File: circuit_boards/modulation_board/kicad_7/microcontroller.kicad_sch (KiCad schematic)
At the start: 27 parts, among them J301 SWD_header, U1 STM32L412K8Ux, U2 VO0600T, U3 SN74LV1T34DBV, Y301 32_768KHZ

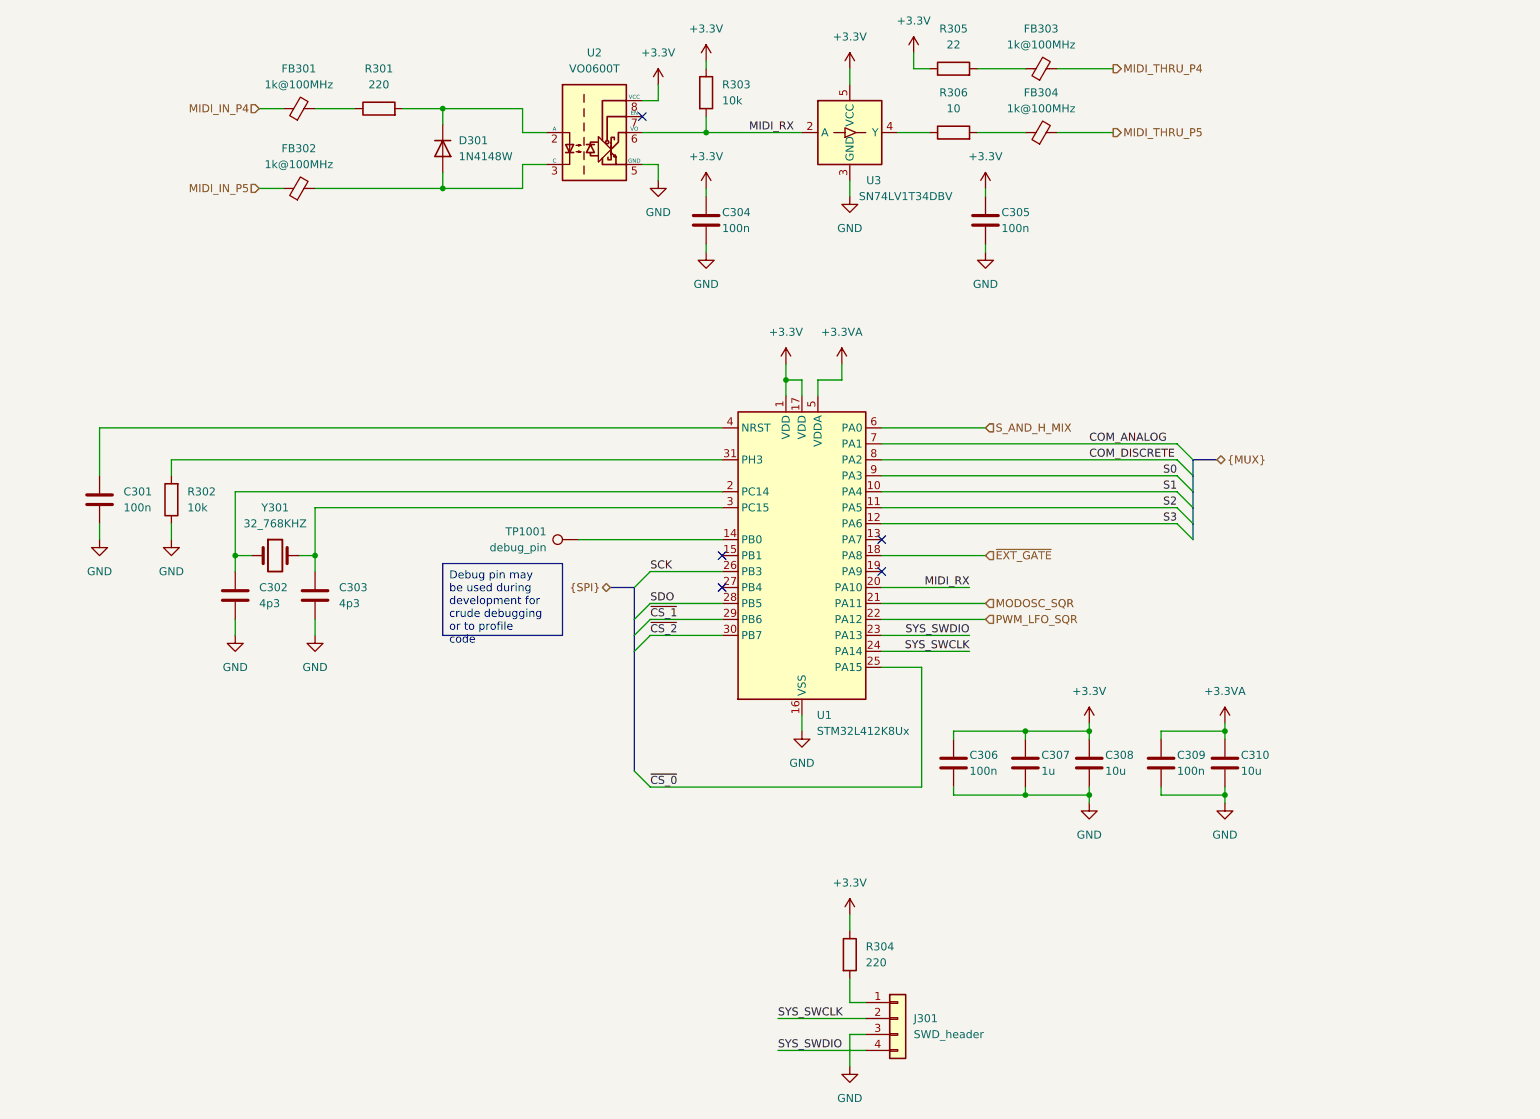
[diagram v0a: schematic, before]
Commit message: Tweaks to mod board, debounce MODOSC toggle switch
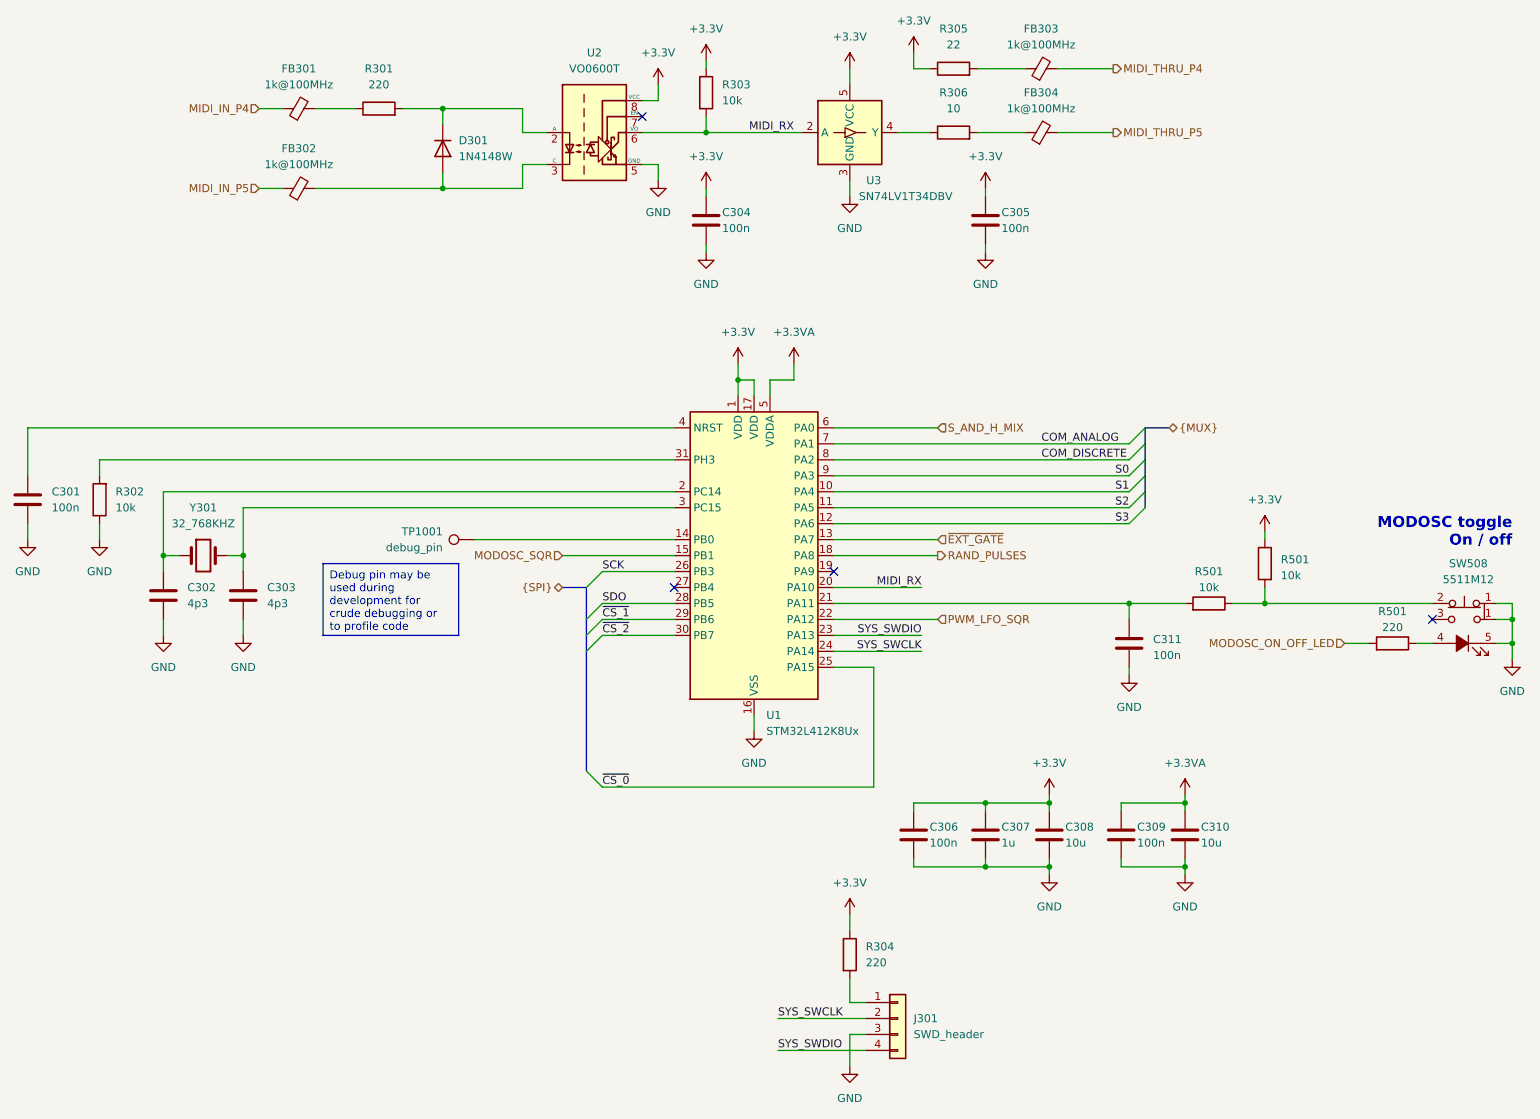
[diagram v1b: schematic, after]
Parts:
- removed U1: STM32L412K8Ux, Package_DFN_QFN:QFN-32-1EP_5x5mm_P0.5mm_EP3.45x3.45mm, symbol MCU_ST_STM32L4:STM32L412K8Ux
- added C311: 100n, Capacitor_SMD:C_0603_1608Metric, symbol Device:C
- added R501 (x2): 10k, Resistor_SMD:R_0603_1608Metric, symbol Device:R
- added R501: 220, Resistor_SMD:R_0603_1608Metric, symbol Device:R
- added SW508: 5511M12, custom_footprints:E_Switch_5511M12, symbol custom_symbols:E_Switch_5511M12
- added U1: STM32L412K8Ux, Package_DFN_QFN:QFN-32-1EP_5x5mm_P0.5mm_EP3.45x3.45mm, symbol custom_symbols:STM32L412K8Ux
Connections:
- net +3.3V: now also R501.1, U1.1 (VDD), U1.17 (VDD)
- net +3.3VA: now also U1.5 (VDDA)
- net COM_ANALOG: now also U1.7 (PA1)
- net COM_DISCRETE: now also U1.8 (PA2)
- net GND: now also C311.1, SW508.1, SW508.5, U1.16 (VSS), U1.32 (VSS), U1.33 (VSS)
- net MIDI_RX: now also U1.20 (PA10)
- net MODOSC_SQR: now also U1.15 (PB1)
- net PWM_LFO_SQR: now also U1.22 (PA12)
- net S0: now also U1.9 (PA3)
- net S1: now also U1.10 (PA4)
- net S2: now also U1.11 (PA5)
- net S3: now also U1.12 (PA6)
- net SCK: now also U1.26 (PB3)
- net SDO: now also U1.28 (PB5)
- net SYS_SWCLK: now also U1.24 (PA14)
- net SYS_SWDIO: now also U1.23 (PA13)
- net S_AND_H_MIX: now also U1.6 (PA0)
- net ~{CS_0}: now also U1.25 (PA15)
- net ~{CS_1}: now also U1.29 (PB6)
- net ~{CS_2}: now also U1.30 (PB7)
- net ~{EXT_GATE}: now also U1.13 (PA7)
- net at C301.2: now also U1.4 (NRST)
- net at R302.2: now also U1.31 (PH3)
- net at C303.2, Y301.2: now also U1.3 (PC15)
- net at C302.2, Y301.1: now also U1.2 (PC14)
- net at TP1001.1: now also U1.14 (PB0)
- new net: R501.1, R501.2, SW508.2
- new net: R501.1, SW508.4
- new net: C311.2, R501.2, U1.21 (PA11)
- new net MODOSC_ON_OFF_LED: R501.2
- new net RAND_PULSES: U1.18 (PA8)
- no-connect marks 5 -> 4
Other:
- note added: "MODOSC toggle On / off"
- moved on the sheet: C301, C302, C303, C306, C307, C308, C309, C310, R302, TP1001, Y301

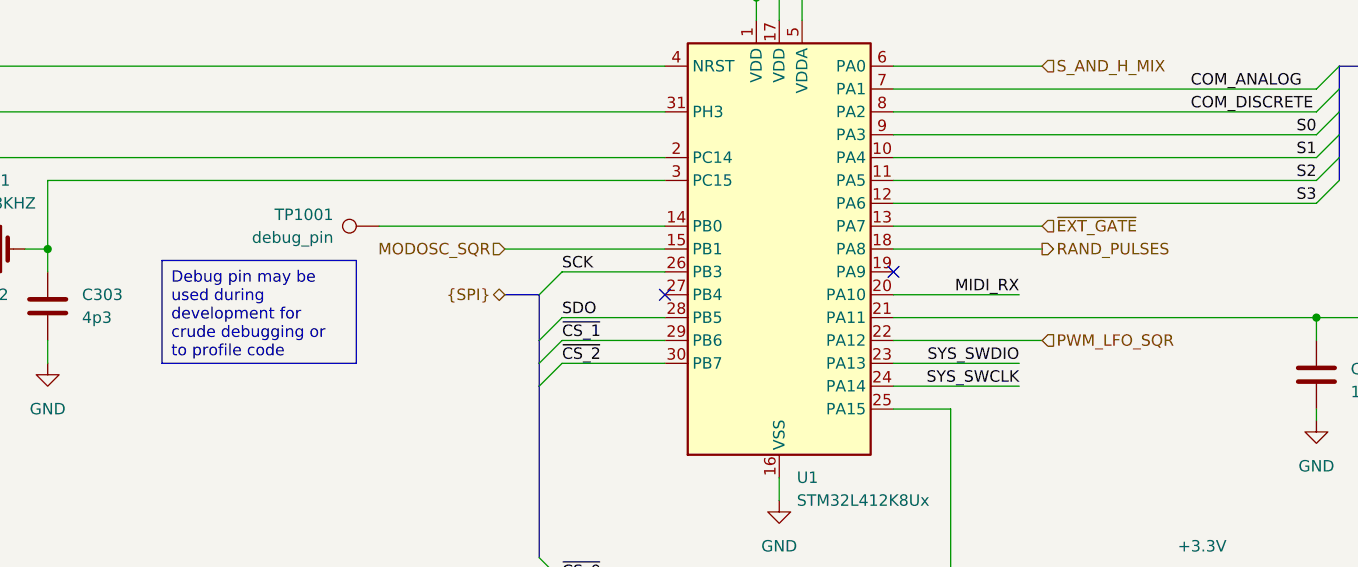
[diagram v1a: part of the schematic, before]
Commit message: Swap some pins on MOD board for independent EXTI lines
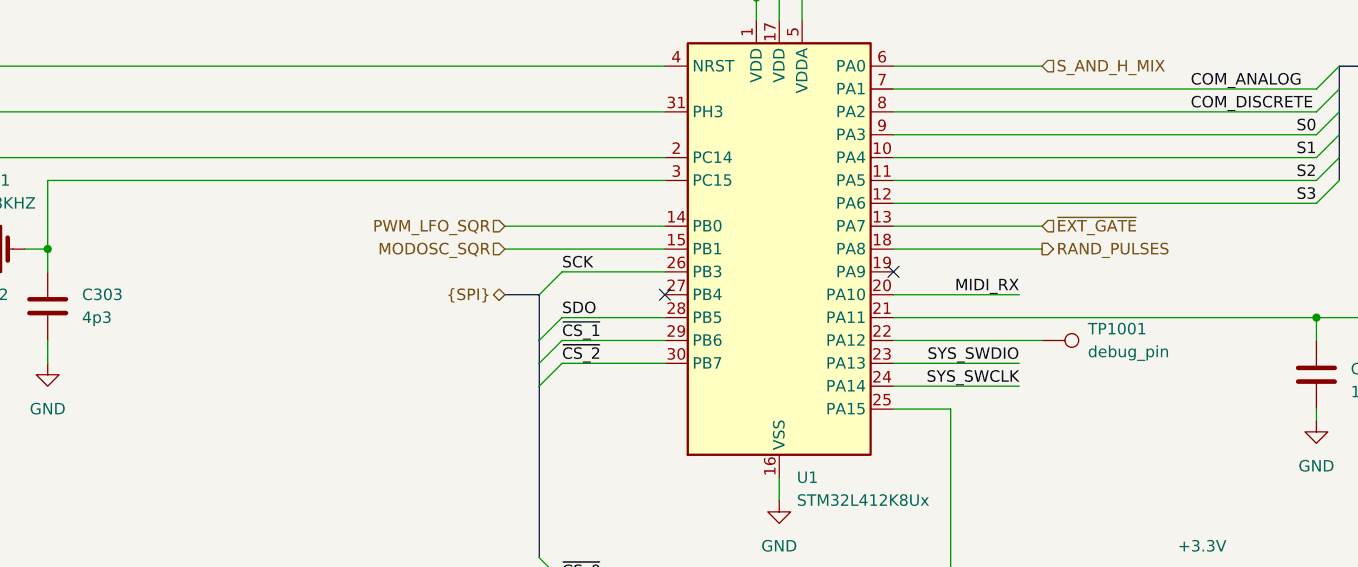
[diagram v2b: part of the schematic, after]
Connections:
- net PWM_LFO_SQR: now also U1.14 (PB0); no longer U1.22 (PA12)
- net at TP1001.1: now also U1.22 (PA12); no longer U1.14 (PB0)
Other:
- moved on the sheet: TP1001
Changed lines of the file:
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@@
   (title_block
     (title "MICRO-OX Modulation Board")
-    (date "2023-04-20")
+    (date "2023-04-21")
     (rev "0")
     (comment 2 "creativecommons.org/licenses/by/4.0")
@@
     (stroke (width 0) (type default))
   )
-  (wire (pts (xy 92.71 102.87) (xy 124.46 102.87))
+  (wire (pts (xy 106.68 102.87) (xy 124.46 102.87))
     (stroke (width 0) (type default))
   )
@@
   (wire (pts (xy 257.81 113.03) (xy 255.27 113.03))
     (stroke (width 0) (type default))
-  )
-  (text_box "Debug pin may be used during development for crude debugging or to profile code"
-    (at 68.58 106.68 0) (size 21.59 11.43)
-    (stroke (width 0) (type default))
-    (fill (type none))
-    (effects (font (size 1.27 1.27)) (justify left top))
   )
   (text "MODOSC toggle\nOn / off" (at 257.81 104.14 0)
@@
     (effects (font (size 1.27 1.27)) (justify left))
   )
-  (hierarchical_label "PWM_LFO_SQR" (shape input) (at 166.37 115.57 0) (fields_autoplaced)
-    (effects (font (size 1.27 1.27)) (justify left))
+  (hierarchical_label "PWM_LFO_SQR" (shape input) (at 106.68 102.87 180) (fields_autoplaced)
+    (effects (font (size 1.27 1.27)) (justify right))
   )
   (hierarchical_label "MODOSC_ON_OFF_LED" (shape input) (at 231.14 119.38 180) (fields_autoplaced)
@@
     )
   )
-  (symbol (lib_id "Connector:TestPoint") (at 92.71 102.87 90) (unit 1)
+  (symbol (lib_id "Connector:TestPoint") (at 166.37 115.57 270) (mirror x) (unit 1)
     (in_bom no) (on_board yes) (dnp no) (fields_autoplaced)
-    (property "Reference" "TP1001" (at 87.63 101.6 90)
-      (effects (font (size 1.27 1.27)) (justify left))
-    )
-    (property "Value" "debug_pin" (at 87.63 104.14 90)
-      (effects (font (size 1.27 1.27)) (justify left))
-    )
-    (property "Footprint" "TestPoint:TestPoint_Keystone_5000-5004_Miniature" (at 92.71 97.79 0)
-      (effects (font (size 1.27 1.27)) hide)
-    )
-    (property "Datasheet" "~" (at 92.71 97.79 0)
-      (effects (font (size 1.27 1.27)) hide)
-    )
+    (property "Reference" "TP1001" (at 171.45 114.3 90)
+      (effects (font (size 1.27 1.27)) (justify left))
+    )
+    (property "Value" "debug_pin" (at 171.45 116.84 90)
+      (effects (font (size 1.27 1.27)) (justify left))
+    )
+    (property "Footprint" "TestPoint:TestPoint_Keystone_5000-5004_Miniature" (at 166.37 110.49 0)
+      (effects (font (size 1.27 1.27)) hide)
+    )
+    (property "Datasheet" "~" (at 166.37 110.49 0)
+      (effects (font (size 1.27 1.27)) hide)
+    )

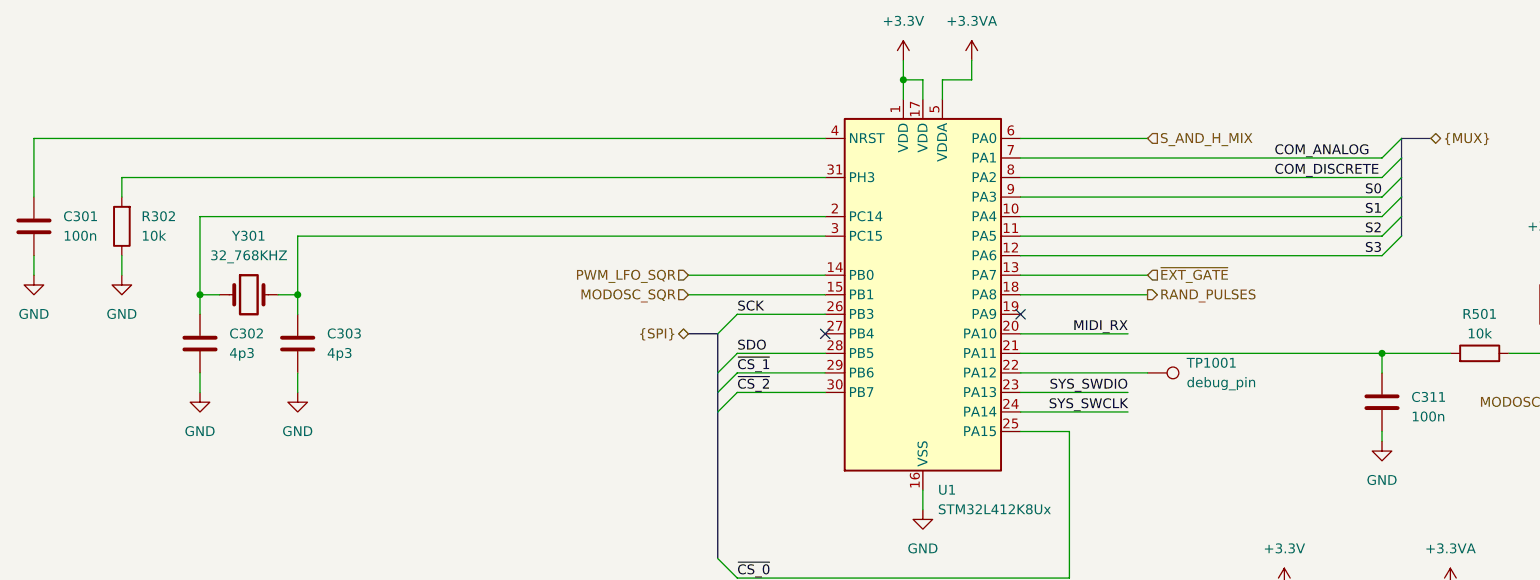
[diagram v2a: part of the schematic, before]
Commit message: Update PCBs, tweak vals, add VCF CV from DAC
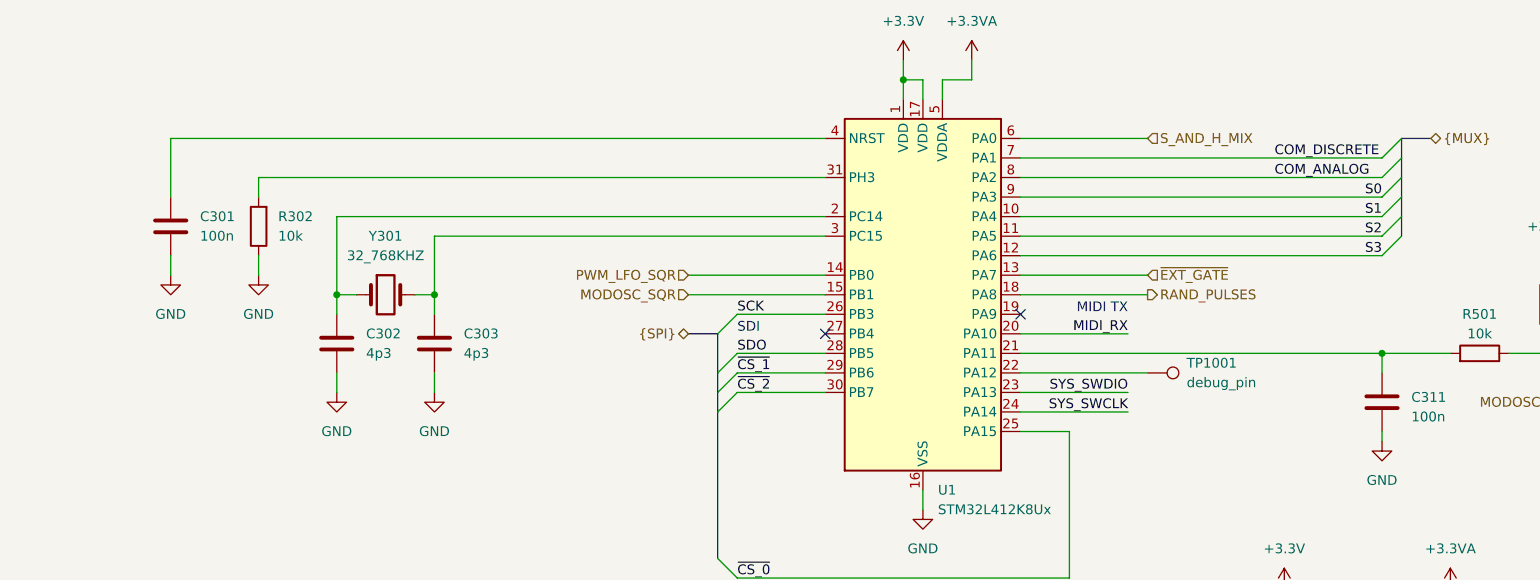
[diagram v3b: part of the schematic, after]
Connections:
- net COM_ANALOG: now also U1.8 (PA2); no longer U1.7 (PA1)
- net COM_DISCRETE: now also U1.7 (PA1); no longer U1.8 (PA2)
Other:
- note added: "MIDI TX"
- note added: "SDI"
- moved on the sheet: C301, C302, C303, R302, Y301
